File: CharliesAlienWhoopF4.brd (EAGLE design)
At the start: 29 x 29 mm, 41 parts, among them M1 53047-0210, M2 53047-0210, M3 53047-0210, M4 53047-0210, Q1 FDMA410NZ, Q2 FDMA410NZ, Q3 IRLML6402, Q4 FDMA410NZ, Q5 FDMA410NZ, U1 MPU-9250, U2 TPS63001, Y1 8mhz

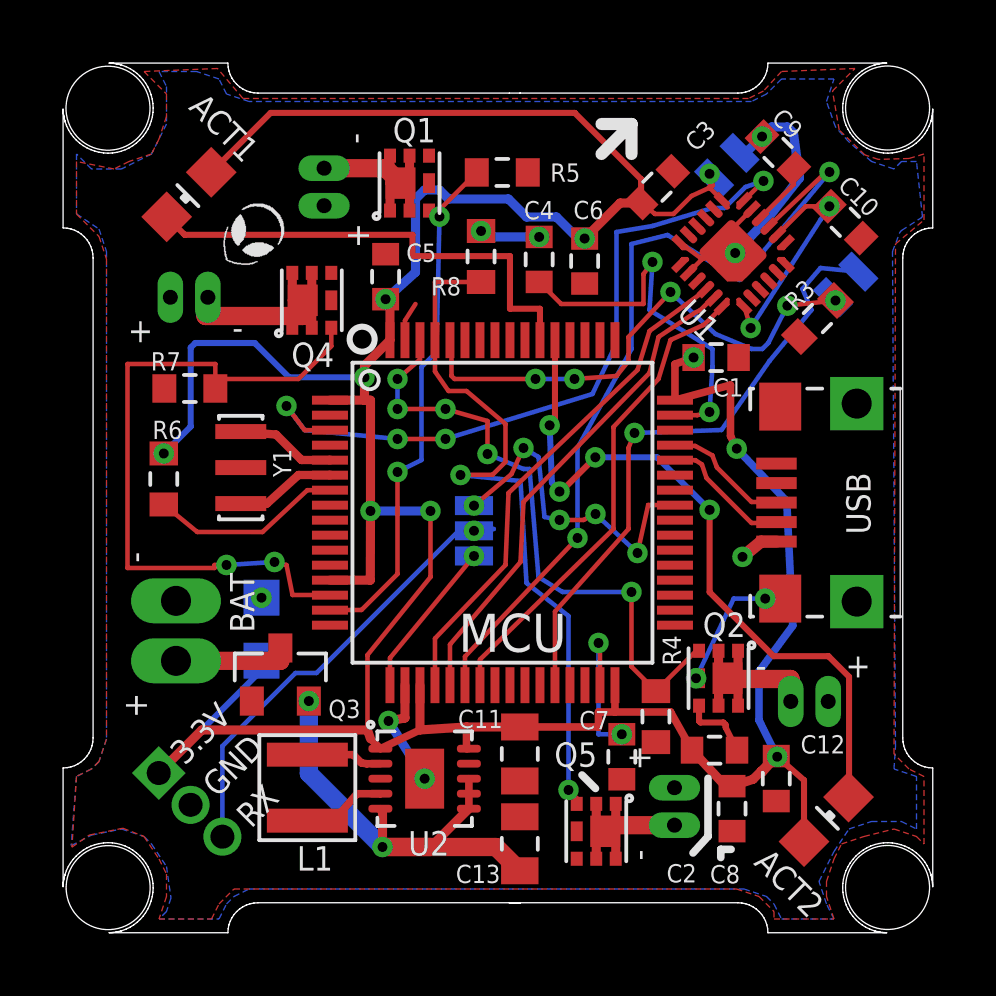
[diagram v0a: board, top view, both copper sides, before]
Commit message: Fixed issue #1 mounting holes not drilled/cut. Thanks to advice from OSH Park's Dan Sheadel I'm now using an actual drill command and have redrawn the outline from scratch and am now cutting across the drill hole for a hopefully cleaner and always cut properly mounting hole set.
Moved R3 silkscreen label since it was being hidden by a via.

Ran ERC and DRC etc all passed. -CKS
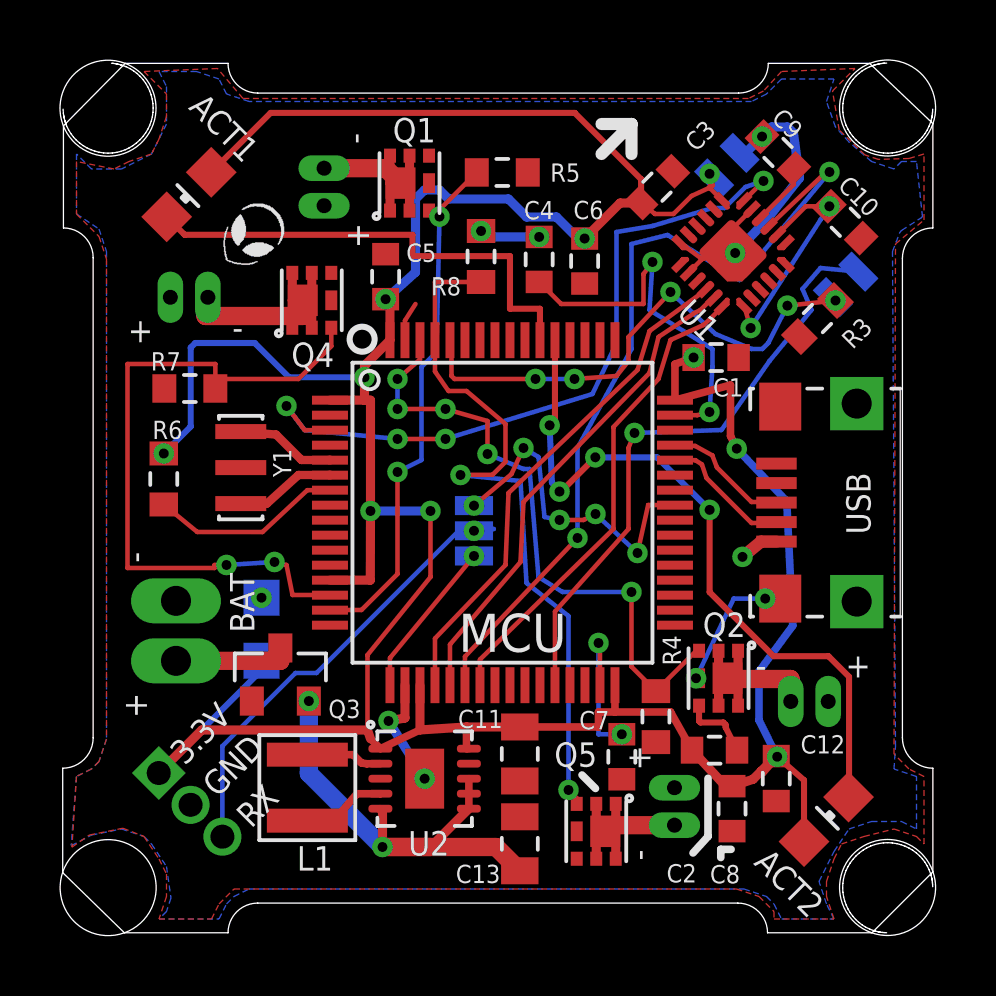
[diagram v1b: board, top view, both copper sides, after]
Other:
- outline, holes or cut-outs redrawn
- board text added: "20170424_0027-STEVENSON REMIX OF ALIENFLIGHT F4 LICENSE: CC BY-NC-SA 4.0"
- board text removed: "20170321_1034-STEVENSON REMIX OF ALIENFLIGHT F4 LICENSE: CC BY-NC-SA 4.0"
